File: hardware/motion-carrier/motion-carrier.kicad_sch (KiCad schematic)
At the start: 8 parts, among them J1 ESP32 devkit left row, J2 ESP32 devkit right row, J3 5V IN from buck, J4 TB6600 PUL+ PUL- DIR+ DIR- EN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, J5 RELAY +5V GND IN, J6 HOME GND TOP GND DRV_ALM GND, J7 PROBE GND FOOT GND STOP GND, J8 LINK to panel: GND TX RX

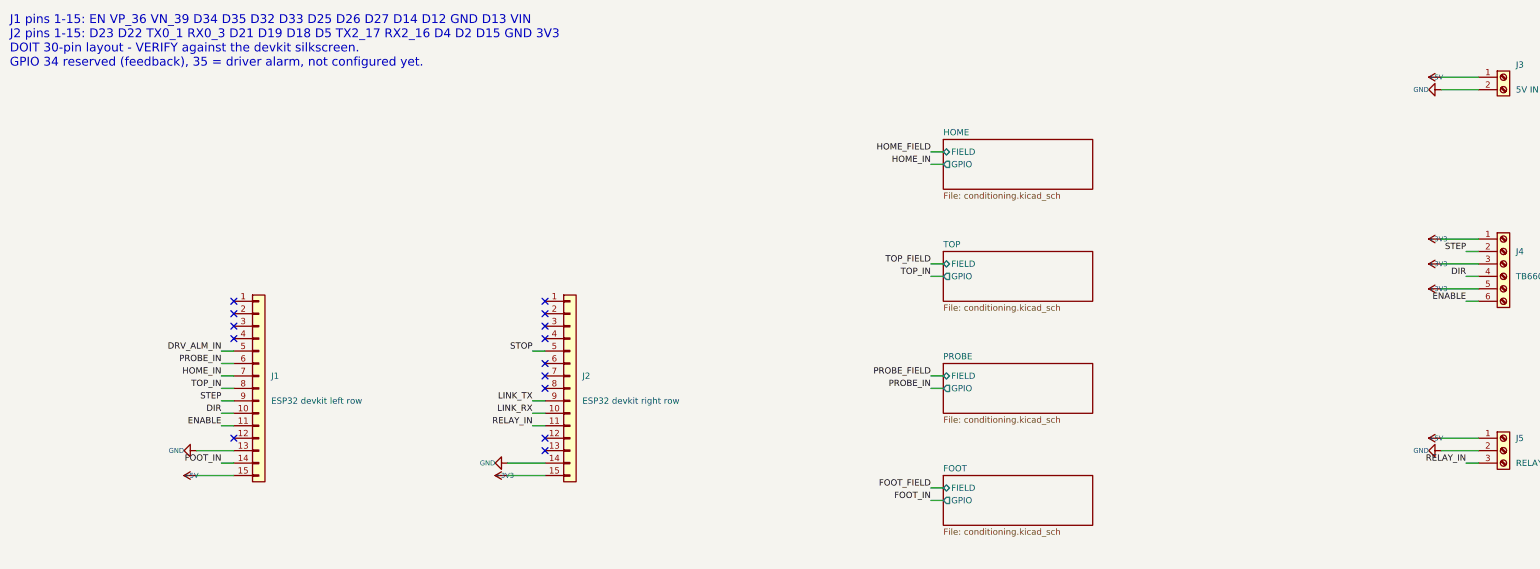
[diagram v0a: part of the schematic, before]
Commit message: fix(hardware): regenerate schematics, symbol library and PDFs
Regenerated output of the preceding fix-wave commits (contactor topology,
devkit pin order, field_gap/arrow-legibility fixes, 74LVC14 fields,
zero-length wire removal). ERC clean (0 violations on all three projects)
and check_pins reports 0 mismatches.

Co-Authored-By: Claude Opus 5 (1M context) <noreply@anthropic.com>
Claude-Session: https://claude.ai/code/session_01N1nWXzYgvFT6pqfHGhLK6P
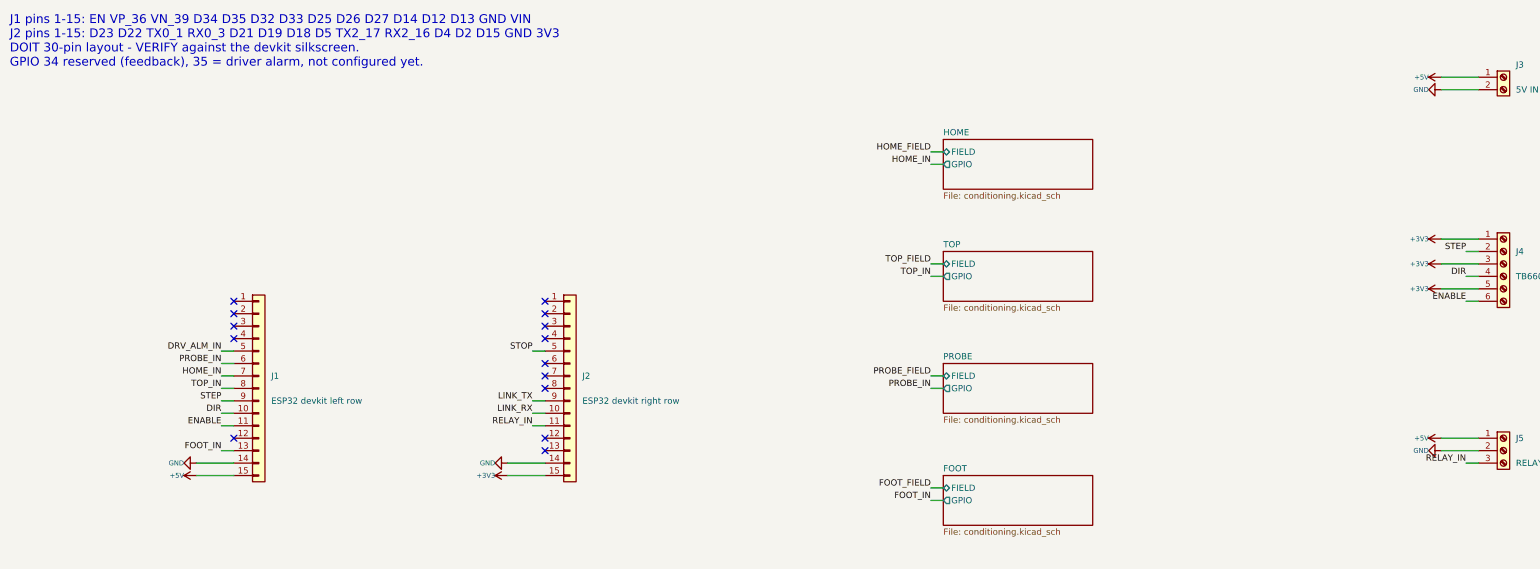
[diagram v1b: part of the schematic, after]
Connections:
- net FOOT_IN: now also J1.13 (Pin_13); no longer J1.14 (Pin_14)
- net GND: now also J1.14 (Pin_14); no longer J1.13 (Pin_13)
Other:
- note added: "J1 pins 1-15: EN VP_36 VN_39 D34 D35 D32 D33 D25 D26 D27 D14 D12 D13 GND VIN J2 pins 1-15: D23 D22 TX0_1 RX0_3 D21 D19 D18 D5 TX2_17 RX2_16 D4 D2 D15 GND 3V3 DOIT 30-pin layout - VERIFY against the devkit silkscreen. GPIO 34 reserved (feedback), 35 = driver alarm, not configured yet."
- note removed: "J1 pins 1-15: EN VP_36 VN_39 D34 D35 D32 D33 D25 D26 D27 D14 D12 GND D13 VIN J2 pins 1-15: D23 D22 TX0_1 RX0_3 D21 D19 D18 D5 TX2_17 RX2_16 D4 D2 D15 GND 3V3 DOIT 30-pin layout - VERIFY against the devkit silkscreen. GPIO 34 reserved (feedback), 35 = driver alarm, not configured yet."
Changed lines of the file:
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@@
 		(pts
 			(xy 71.12 114.3)
-			(xy 63.5 114.3))
-		(stroke
-			(width 0)
-			(type default))
+			(xy 68.58 114.3))
+		(stroke
+			(width 0)
+			(type default))
+)
+	(label "FOOT_IN"
+		(at 68.58 114.3 180)
+		(effects
+			(font
+				(size 1.27 1.27))
+			(justify right bottom))
 )
 	(wire
 		(pts
 			(xy 71.12 116.84)
-			(xy 68.58 116.84))
-		(stroke
-			(width 0)
-			(type default))
-)
-	(label "FOOT_IN"
-		(at 68.58 116.84 180)
-		(effects
-			(font
-				(size 1.27 1.27))
-			(justify right bottom))
+			(xy 63.5 116.84))
+		(stroke
+			(width 0)
+			(type default))
 )
 	(wire
@@
 			(type default))
 )
-	(text "J1 pins 1-15: EN VP_36 VN_39 D34 D35 D32 D33 D25 D26 D27 D14 D12 GND D13 VIN\nJ2 pins 1-15: D23 D22 TX0_1 RX0_3 D21 D19 D18 D5 TX2_17 RX2_16 D4 D2 D15 GND 3V3\nDOIT 30-pin layout - VERIFY against the devkit silkscreen.\nGPIO 34 reserved (feedback), 35 = driver alarm, not configured yet."
+	(text "J1 pins 1-15: EN VP_36 VN_39 D34 D35 D32 D33 D25 D26 D27 D14 D12 D13 GND VIN\nJ2 pins 1-15: D23 D22 TX0_1 RX0_3 D21 D19 D18 D5 TX2_17 RX2_16 D4 D2 D15 GND 3V3\nDOIT 30-pin layout - VERIFY against the devkit silkscreen.\nGPIO 34 reserved (feedback), 35 = driver alarm, not configured yet."
 		(exclude_from_sim no)
 		(at 25.4 25.4 0)
@@
 	(symbol
 		(lib_id "power:GND")
-		(at 63.5 114.3 270)
+		(at 63.5 116.84 270)
 		(unit 1)
 		(exclude_from_sim no)
@@
 		(dnp no)
 		(property "Reference" "#PWR1"
-			(at 66.04 111.76 90)
+			(at 66.04 114.3 90)
 			(effects
 				(font
@@
 				(hide yes)))
 		(property "Value" "GND"
-			(at 60.96 114.3 90)
+			(at 60.96 116.84 90)
 			(effects
 				(font
@@
 				(justify right)))
 		(property "Footprint" ""
-			(at 63.5 114.3 90)
-			(effects
-				(font
-					(size 1.27 1.27))
-				(justify left)
-				(hide yes)))
-		(property "Datasheet" ""
-			(at 63.5 114.3 90)
+			(at 63.5 116.84 90)
+			(effects
+				(font
+					(size 1.27 1.27))
+				(justify left)
+				(hide yes)))
+		(property "Datasheet" ""
+			(at 63.5 116.84 90)
 			(effects
 				(font
@@
 				(font
 					(size 1 1))
-				(justify right)))
+				(justify left)))
 		(property "Footprint" ""
 			(at 63.5 119.38 90)
@@
 				(font
 					(size 1 1))
-				(justify right)))
+				(justify left)))
 		(property "Footprint" ""
 			(at 127 119.38 90)
@@
 				(font
 					(size 1 1))
-				(justify right)))
+				(justify left)))
 		(property "Footprint" ""
 			(at 317.5 38.1 90)
@@
 				(font
 					(size 1 1))
-				(justify right)))
+				(justify left)))
 		(property "Footprint" ""
 			(at 317.5 71.12 90)
@@
 				(font
 					(size 1 1))
-				(justify right)))
+				(justify left)))
 		(property "Footprint" ""
 			(at 317.5 76.2 90)
@@
 				(font
 					(size 1 1))
-				(justify right)))
+				(justify left)))
 		(property "Footprint" ""
 			(at 317.5 81.28 90)
@@
 				(font
 					(size 1 1))
-				(justify right)))
+				(justify left)))
 		(property "Footprint" ""
 			(at 317.5 111.76 90)

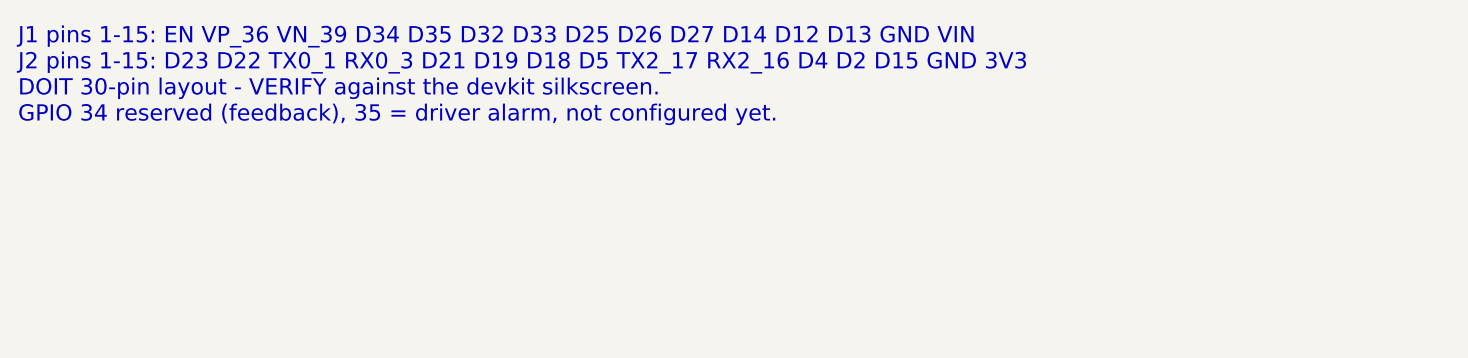
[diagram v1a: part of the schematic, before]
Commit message: docs(hardware): mark the devkit header rows verified against the HW-394 board
Both 30-pin header rows match the silkscreen of the board in hand
(HW-394, CH340C, USB-C). Use its D17/D16 labels for the UART2 pins and
drop the open item from hardware/README.md.

Co-Authored-By: Claude Opus 5 (1M context) <noreply@anthropic.com>
Claude-Session: https://claude.ai/code/session_01N1nWXzYgvFT6pqfHGhLK6P
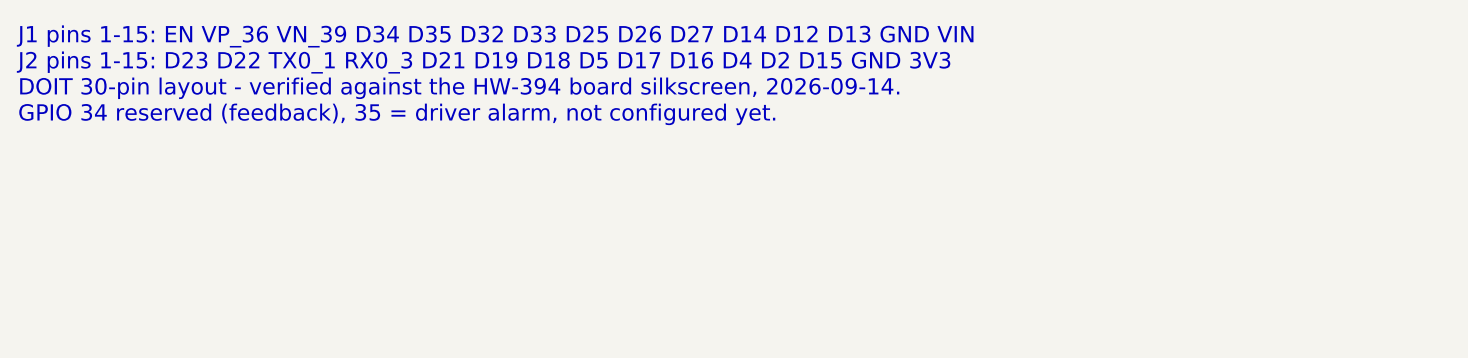
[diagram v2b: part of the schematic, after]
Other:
- note added: "J1 pins 1-15: EN VP_36 VN_39 D34 D35 D32 D33 D25 D26 D27 D14 D12 D13 GND VIN J2 pins 1-15: D23 D22 TX0_1 RX0_3 D21 D19 D18 D5 D17 D16 D4 D2 D15 GND 3V3 DOIT 30-pin layout - verified against the HW-394 board silkscreen, 2026-09-14. GPIO 34 reserved (feedback), 35 = driver alarm, not configured yet."
- note removed: "J1 pins 1-15: EN VP_36 VN_39 D34 D35 D32 D33 D25 D26 D27 D14 D12 D13 GND VIN J2 pins 1-15: D23 D22 TX0_1 RX0_3 D21 D19 D18 D5 TX2_17 RX2_16 D4 D2 D15 GND 3V3 DOIT 30-pin layout - VERIFY against the devkit silkscreen. GPIO 34 reserved (feedback), 35 = driver alarm, not configured yet."
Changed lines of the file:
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@@
 			(type default))
 )
-	(text "J1 pins 1-15: EN VP_36 VN_39 D34 D35 D32 D33 D25 D26 D27 D14 D12 D13 GND VIN\nJ2 pins 1-15: D23 D22 TX0_1 RX0_3 D21 D19 D18 D5 TX2_17 RX2_16 D4 D2 D15 GND 3V3\nDOIT 30-pin layout - VERIFY against the devkit silkscreen.\nGPIO 34 reserved (feedback), 35 = driver alarm, not configured yet."
+	(text "J1 pins 1-15: EN VP_36 VN_39 D34 D35 D32 D33 D25 D26 D27 D14 D12 D13 GND VIN\nJ2 pins 1-15: D23 D22 TX0_1 RX0_3 D21 D19 D18 D5 D17 D16 D4 D2 D15 GND 3V3\nDOIT 30-pin layout - verified against the HW-394 board silkscreen, 2026-09-14.\nGPIO 34 reserved (feedback), 35 = driver alarm, not configured yet."
 		(exclude_from_sim no)
 		(at 25.4 25.4 0)
